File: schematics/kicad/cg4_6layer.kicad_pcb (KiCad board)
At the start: 6 copper layers, 148.8 x 225.9 mm, 137 parts, among them J7 DE15_Socket_HighDensity, K1300 10uF, P4 DIN41612_03x32_C_Split, U1000 PAL16R8, U1001 PAL20X10, U1002 PAL20X10, U1003 PAL20X10, U1004 PAL20R6, U1005 P16L8, U1006 PAL16R8, U1007 P20L8, U1008 P16L8, U1009 P16L8, U1010 P16L8, U1015 74F175, U1016 74F244, U1017 330Ω, U1021 330Ω, U1036 330Ω, U1037 330Ω, U1038 330Ω, U1100 74F257, U1101 74F257, U1102 74F257, U1103 74F257, U1104 330Ω, U1105 330Ω, U1110 74F257, U1111 74F257, U1112 74F257, U1113 74F257, U1114 330Ω, U1129 74LS393, U1200 HM53461, U1201 HM53461, U1202 HM53461, U1203 HM53461, U1204 HM53461, U1205 HM53461, U1206 HM53461, U1207 HM53461, U1208 HM53461, U1209 HM53461, U1210 HM53461, U1211 HM53461, U1212 HM53461, U1213 HM53461, U1214 HM53461, U1215 HM53461, U1216 HM53461, U1217 HM53461, U1218 HM53461, U1219 HM53461, U1220 HM53461, U1221 HM53461, U1222 HM53461, U1223 HM53461, U1224 HM53461, U1225 HM53461, U1226 HM53461, U1227 HM53461, U1228 HM53461, U1229 HM53461, U1230 HM53461, U1231 HM53461, U1300 HM53461, U1301 HM53461, U1302 HM53461, U1303 HM53461, U1304 HM53461, U1305 HM53461, U1306 HM53461, U1307 HM53461, U1310 BT458, U1311 92.9405Mhz, U1312 10H101, U1313 10H131, U1314 10H350, U1315 LM385BZ-1.2, U1318 74F08

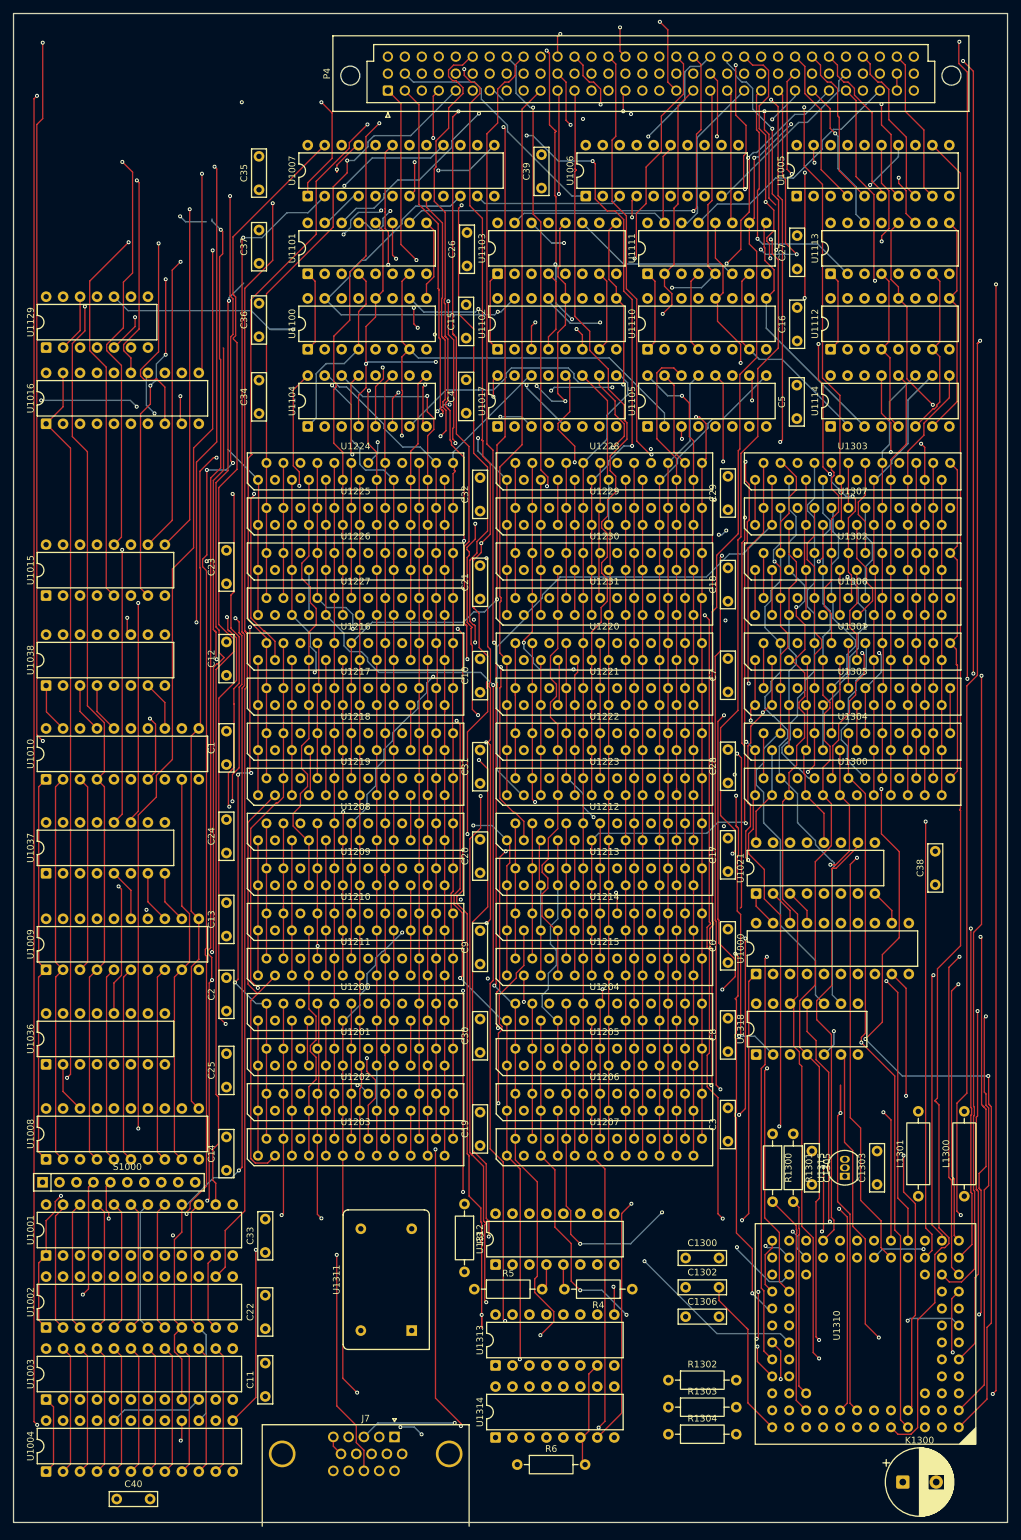
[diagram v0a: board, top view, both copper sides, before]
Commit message: More fixes from the physical board tracing. Playing around with layouts: main "cg4" layout is relaxed so it can autoroute. 6layer is the original layout, and the ram_routed is a partial/manually routed version, less relaxed than the main one.
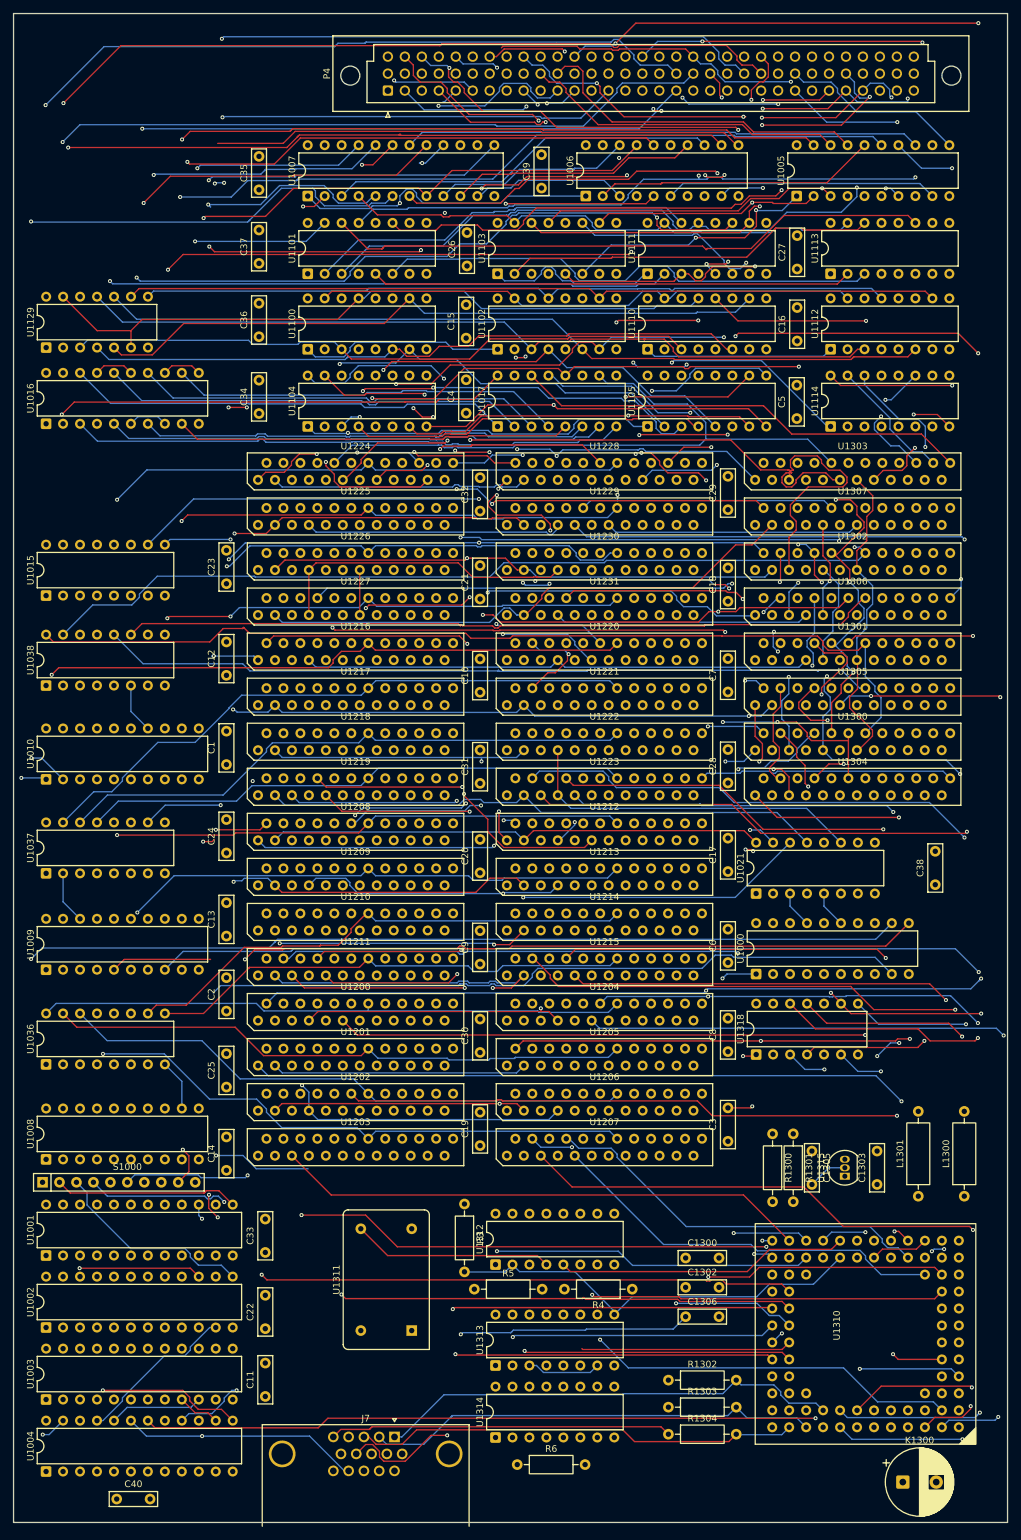
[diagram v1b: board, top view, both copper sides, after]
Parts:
- moved U1304 6.75 mm to (164.9, 162.7)
- moved U1300 6.75 mm to (164.9, 155.9)
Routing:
- net /Misc/EN.VIDEO: track 0.00 -> 317.7 mm, vias 0 -> 2
- net /Misc/D27: track 187.5 -> 396.5 mm, vias 3 -> 6
- net /Misc/SIZ0: track 58.7 -> 266.2 mm, vias 0 -> 2
- net /Misc/SIZ1: track 58.7 -> 259.0 mm, vias 0 -> 2
- net /Video Control/V.UNK2: track 15.3 -> 200.8 mm, vias 2 -> 1
- net /Misc/D17: track 33.3 -> 204.4 mm, vias 1 -> 4
- net /Video Output/V.D.D0: track 179.5 -> 20.2 mm, vias 2 -> 0
- net /Video Control/V.CLR: track 16.4 -> 171.4 mm
- net /Video Output/V.D.D3: track 171.7 -> 47.6 mm, vias 3 -> 1
- net /Video Output/V.C.D4: track 169.0 -> 45.5 mm, vias 3 -> 1
- net /Video Output/V.B.D5: track 21.3 -> 138.2 mm, vias 0 -> 2
- net /Misc/D23: track 261.9 -> 151.8 mm, vias 5 -> 4
- net /Misc/D14: track 138.2 -> 30.9 mm, vias 3 -> 1
- net /Misc/D18: track 184.6 -> 80.2 mm, vias 3 -> 2
- net /Misc/D8: track 21.3 -> 125.1 mm, vias 1 -> 7
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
